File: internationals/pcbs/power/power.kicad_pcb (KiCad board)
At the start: 2 copper layers, 39 x 42 mm, 10 parts, among them J1 XT60E-M, J2 XT60E-M, J3 XT30-F, J4 XT30-F, J5 JST-XH-B4B, J6 JST-XH-S4B

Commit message: pcbs: power: feat: complete solder mask and silkscreen
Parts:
- added G***: LOGO, LOGO, F.Cu at (100.0, 167.0)
- added G***: LOGO, LOGO, F.Cu at (113.9, 146.4)
- added G***: LOGO, LOGO, F.Cu at (102.0, 165.0)
- added kibuzzard-66701961: G***, kibuzzard-66701961, F.Cu at (97.0, 161.4)
- added kibuzzard-66701961: G***, kibuzzard-66701961, B.Cu at (97.0, 169.5)
- added kibuzzard-66701992: G***, kibuzzard-66701992, F.Cu at (112.4, 169.4)
- added kibuzzard-66701992: G***, kibuzzard-66701992, B.Cu at (111.0, 169.4)
- added kibuzzard-667019FA: G***, kibuzzard-667019FA, F.Cu at (97.0, 139.0)
- added kibuzzard-667019FA: G***, kibuzzard-667019FA, B.Cu at (97.0, 140.5)
- added kibuzzard-66701A06: G***, kibuzzard-66701A06, F.Cu at (81.0, 148.0)
- added kibuzzard-66701A06: G***, kibuzzard-66701A06, F.Cu at (113.0, 148.0)
- added kibuzzard-66701A06: G***, kibuzzard-66701A06, B.Cu at (81.0, 148.0)
- added kibuzzard-66701A06: G***, kibuzzard-66701A06, B.Cu at (113.0, 148.0)
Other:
- board text added: "JLCJLCJLCJLC"
- board text added: "Team Gloves Zhou Yikun & Zachary Ang Club Automatica Singapore 2024"

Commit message: pcbs: power: fix: increased copper area and update gerber
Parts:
- removed H1, H2: MountingHole-M3, MountingHole:MountingHole_3.2mm_M3_Pad_Via
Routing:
- net +12V: track 0.00 -> 24.9 mm
- net GND: track 0.00 -> 3.18 mm
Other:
- outline, holes or cut-outs redrawn

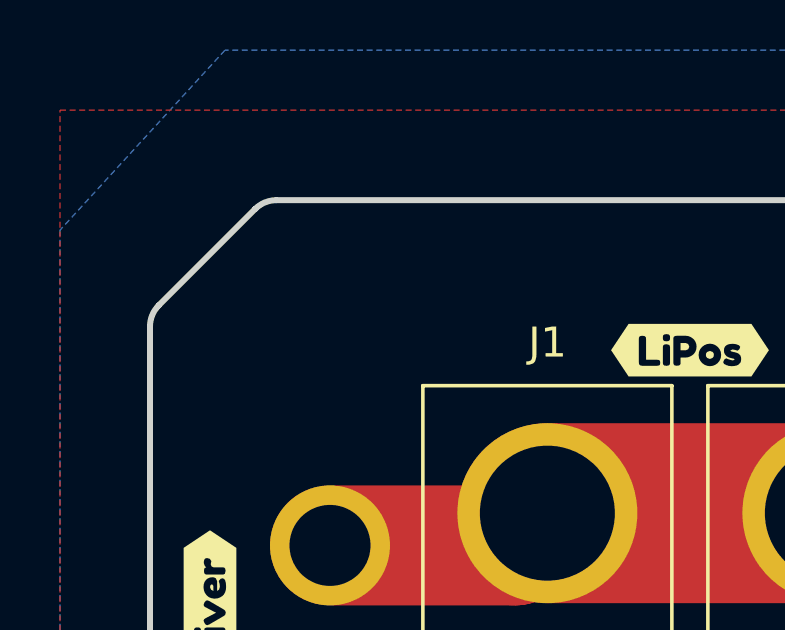
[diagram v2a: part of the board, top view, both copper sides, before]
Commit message: pcbs: feat: add OSHW and Rust Ferris logos
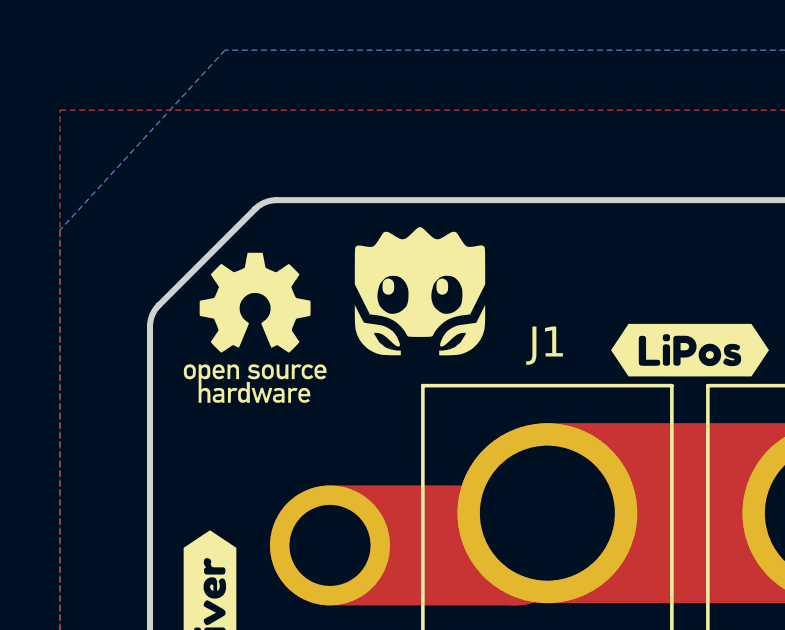
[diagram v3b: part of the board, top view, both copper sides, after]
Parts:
- added G***: LOGO, LOGO, F.Cu at (82.5, 138.2)
- added G***: LOGO, LOGO, F.Cu at (88.0, 137.0)
